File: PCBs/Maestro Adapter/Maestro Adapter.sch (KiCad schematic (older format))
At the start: 14 parts, among them J0 Conn_01x02_Female, J1 Conn_01x02_Female, J10 Conn_01x02_Female, J11 Conn_01x02_Female, J12 Conn_01x12_Male, J13 Conn_01x12_Male, J2 Conn_01x02_Female, J3 Conn_01x02_Female, J4 Conn_01x02_Female, J5 Conn_01x02_Female, J6 Conn_01x02_Female, J7 Conn_01x02_Female, J8 Conn_01x02_Female, J9 Conn_01x02_Female

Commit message: added spot for missed gap in servo channels
missed a gap between channel 5 and 6. so added additional pads
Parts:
- removed J12, J13: Conn_01x12_Male, through hole:1x12 through hole, symbol Connector:Conn_01x12_Male
- added J12, J13: Conn_01x13_Male, through hole:1x13 through hole, symbol Connector:Conn_01x13_Male
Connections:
- wire segments 45 -> 50
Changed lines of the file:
@@
 EESchema Schematic File Version 4
+LIBS:Maestro Adapter-cache
 EELAYER 26 0
 EELAYER END
@@
 $EndDescr
 $Comp
-L Connector:Conn_01x12_Male J13
-U 1 1 5BCE744C
-P 1550 3800
-F 0 "J13" H 1656 4478 50  0000 C CNN
-F 1 "Conn_01x12_Male" H 1656 4387 50  0000 C CNN
-F 2 "through hole:1x12 through hole" H 1550 3800 50  0001 C CNN
-F 3 "~" H 1550 3800 50  0001 C CNN
-	1    1550 3800
-	1    0    0    -1
-$EndComp
-$Comp
-L Connector:Conn_01x12_Male J12
-U 1 1 5BCE74E8
-P 2400 3800
-F 0 "J12" H 2506 4478 50  0000 C CNN
-F 1 "Conn_01x12_Male" H 2506 4387 50  0000 C CNN
-F 2 "through hole:1x12 through hole" H 2400 3800 50  0001 C CNN
-F 3 "~" H 2400 3800 50  0001 C CNN
-	1    2400 3800
-	1    0    0    -1
-$EndComp
-$Comp
 L Connector:Conn_01x02_Female J11
 U 1 1 5BCE7753
@@
 Text GLabel 4150 2700 0    50   Input ~ 0
 GND
-Wire Wire Line
-	1750 3300 1750 3400
-Connection ~ 1750 3400
-Wire Wire Line
-	1750 3400 1750 3500
-Connection ~ 1750 3500
-Wire Wire Line
-	1750 3500 1750 3600
-Connection ~ 1750 3600
-Wire Wire Line
-	1750 3600 1750 3700
-Connection ~ 1750 3700
-Wire Wire Line
-	1750 3700 1750 3800
-Connection ~ 1750 3800
-Wire Wire Line
-	1750 3800 1750 3900
-Connection ~ 1750 3900
-Wire Wire Line
-	1750 3900 1750 4000
-Connection ~ 1750 4000
-Wire Wire Line
-	1750 4000 1750 4100
-Connection ~ 1750 4100
-Wire Wire Line
-	1750 4100 1750 4200
-Connection ~ 1750 4200
-Wire Wire Line
-	1750 4200 1750 4300
-Connection ~ 1750 4300
-Wire Wire Line
-	1750 4300 1750 4400
 Text GLabel 1750 4400 3    50   Input ~ 0
 GND
@@
 Wire Wire Line
 	3250 3400 4150 3400
-Wire Wire Line
-	2600 3800 3350 3800
-Wire Wire Line
-	3350 3800 3350 3600
-Wire Wire Line
-	3350 3600 4150 3600
-Wire Wire Line
-	2600 3900 3450 3900
-Wire Wire Line
-	3450 3900 3450 3800
-Wire Wire Line
-	3450 3800 4150 3800
-Wire Wire Line
-	2600 4000 4150 4000
-Wire Wire Line
-	2600 4100 3450 4100
-Wire Wire Line
-	3450 4100 3450 4200
-Wire Wire Line
-	3450 4200 4150 4200
-Wire Wire Line
-	2600 4200 3350 4200
-Wire Wire Line
-	3350 4200 3350 4400
-Wire Wire Line
-	3350 4400 4150 4400
-Wire Wire Line
-	2600 4300 3250 4300
-Wire Wire Line
-	3250 4300 3250 4600
-Wire Wire Line
-	3250 4600 4150 4600
-Wire Wire Line
-	2600 4400 3150 4400
-Wire Wire Line
-	3150 4400 3150 4800
-Wire Wire Line
-	3150 4800 4150 4800
 $Bitmap
 Pos 9100 6900
@@
 EndData
 $EndBitmap
+$Comp
+L Connector:Conn_01x13_Male J12
+U 1 1 5BCF052F
+P 2400 3900
+F 0 "J12" H 2506 4678 50  0000 C CNN
+F 1 "Conn_01x13_Male" H 2506 4587 50  0000 C CNN
+F 2 "through hole:1x13 through hole" H 2400 3900 50  0001 C CNN
+F 3 "~" H 2400 3900 50  0001 C CNN
+	1    2400 3900
+	1    0    0    -1
+$EndComp
+$Comp
+L Connector:Conn_01x13_Male J13
+U 1 1 5BCF059F
+P 1550 3800
+F 0 "J13" H 1656 4578 50  0000 C CNN
+F 1 "Conn_01x13_Male" H 1656 4487 50  0000 C CNN
+F 2 "through hole:1x13 through hole" H 1550 3800 50  0001 C CNN
+F 3 "~" H 1550 3800 50  0001 C CNN
+	1    1550 3800
+	1    0    0    -1
+$EndComp
+Wire Wire Line
+	2600 4500 2800 4500
+Wire Wire Line
+	2800 4500 2800 4800
+Wire Wire Line
+	2800 4800 4150 4800
+Wire Wire Line
+	2600 4400 2900 4400
+Wire Wire Line
+	2900 4400 2900 4600
+Wire Wire Line
+	2900 4600 4150 4600
+Wire Wire Line
+	2600 4300 3000 4300
+Wire Wire Line
+	3000 4300 3000 4400
+Wire Wire Line
+	3000 4400 4150 4400
+Wire Wire Line
+	2600 4200 4150 4200
+Wire Wire Line
+	2600 4100 3000 4100
+Wire Wire Line
+	3000 4100 3000 4000
+Wire Wire Line
+	3000 4000 4150 4000
+Wire Wire Line
+	2600 4000 2950 4000
+Wire Wire Line
+	2950 4000 2950 3900
+Wire Wire Line
+	2950 3900 3850 3900
+Wire Wire Line
+	3850 3900 3850 3800
+Wire Wire Line
+	3850 3800 4150 3800
+Wire Wire Line
+	2600 3900 2850 3900
+Wire Wire Line
+	2850 3900 2850 3800
+Wire Wire Line
+	2850 3800 3750 3800
+Wire Wire Line
+	3750 3800 3750 3600
+Wire Wire Line
+	3750 3600 4150 3600
+Wire Wire Line
+	1750 3200 1750 3300
+Connection ~ 1750 3300
+Wire Wire Line
+	1750 3300 1750 3400
+Connection ~ 1750 3400
+Wire Wire Line
+	1750 3400 1750 3500
+Connection ~ 1750 3500
+Wire Wire Line
+	1750 3500 1750 3600
+Connection ~ 1750 3600
+Wire Wire Line
+	1750 3600 1750 3700
+Connection ~ 1750 3700
+Wire Wire Line
+	1750 3700 1750 3800
+Connection ~ 1750 3800
+Wire Wire Line
+	1750 3800 1750 3900
+Connection ~ 1750 3900
+Wire Wire Line
+	1750 3900 1750 4000
+Connection ~ 1750 4000
+Wire Wire Line
+	1750 4000 1750 4100
+Connection ~ 1750 4100
+Wire Wire Line
+	1750 4100 1750 4200
+Connection ~ 1750 4200
+Wire Wire Line
+	1750 4200 1750 4300
+Connection ~ 1750 4300
+Wire Wire Line
+	1750 4300 1750 4400
 $EndSCHEMATC

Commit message: Added Colour to 3D Model
We probably have to change the footprint again anyways, but at least now its in colour!!!
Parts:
- J0, J1, J10, J11, J2, J3, J4, J5, J6, J7, J8, J9: footprint through hole:1x2_molex_llc -> EER:1x2_molex_llc
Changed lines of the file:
@@
 F 0 "J11" H 4377 2576 50  0000 L CNN
 F 1 "Conn_01x02_Female" H 4377 2485 50  0000 L CNN
-F 2 "through hole:1x2_molex_llc" H 4350 2600 50  0001 C CNN
+F 2 "EER:1x2_molex_llc" H 4350 2600 50  0001 C CNN
 F 3 "~" H 4350 2600 50  0001 C CNN
 	1    4350 2600
@@
 F 0 "J10" H 4377 2776 50  0000 L CNN
 F 1 "Conn_01x02_Female" H 4377 2685 50  0000 L CNN
-F 2 "through hole:1x2_molex_llc" H 4350 2800 50  0001 C CNN
+F 2 "EER:1x2_molex_llc" H 4350 2800 50  0001 C CNN
 F 3 "~" H 4350 2800 50  0001 C CNN
 	1    4350 2800
@@
 F 0 "J9" H 4377 2976 50  0000 L CNN
 F 1 "Conn_01x02_Female" H 4377 2885 50  0000 L CNN
-F 2 "through hole:1x2_molex_llc" H 4350 3000 50  0001 C CNN
+F 2 "EER:1x2_molex_llc" H 4350 3000 50  0001 C CNN
 F 3 "~" H 4350 3000 50  0001 C CNN
 	1    4350 3000
@@
 F 0 "J8" H 4377 3176 50  0000 L CNN
 F 1 "Conn_01x02_Female" H 4377 3085 50  0000 L CNN
-F 2 "through hole:1x2_molex_llc" H 4350 3200 50  0001 C CNN
+F 2 "EER:1x2_molex_llc" H 4350 3200 50  0001 C CNN
 F 3 "~" H 4350 3200 50  0001 C CNN
 	1    4350 3200
@@
 F 0 "J7" H 4377 3376 50  0000 L CNN
 F 1 "Conn_01x02_Female" H 4377 3285 50  0000 L CNN
-F 2 "through hole:1x2_molex_llc" H 4350 3400 50  0001 C CNN
+F 2 "EER:1x2_molex_llc" H 4350 3400 50  0001 C CNN
 F 3 "~" H 4350 3400 50  0001 C CNN
 	1    4350 3400
@@
 F 0 "J6" H 4377 3576 50  0000 L CNN
 F 1 "Conn_01x02_Female" H 4377 3485 50  0000 L CNN
-F 2 "through hole:1x2_molex_llc" H 4350 3600 50  0001 C CNN
+F 2 "EER:1x2_molex_llc" H 4350 3600 50  0001 C CNN
 F 3 "~" H 4350 3600 50  0001 C CNN
 	1    4350 3600
@@
 F 0 "J5" H 4377 3776 50  0000 L CNN
 F 1 "Conn_01x02_Female" H 4377 3685 50  0000 L CNN
-F 2 "through hole:1x2_molex_llc" H 4350 3800 50  0001 C CNN
+F 2 "EER:1x2_molex_llc" H 4350 3800 50  0001 C CNN
 F 3 "~" H 4350 3800 50  0001 C CNN
 	1    4350 3800
@@
 F 0 "J4" H 4377 3976 50  0000 L CNN
 F 1 "Conn_01x02_Female" H 4377 3885 50  0000 L CNN
-F 2 "through hole:1x2_molex_llc" H 4350 4000 50  0001 C CNN
+F 2 "EER:1x2_molex_llc" H 4350 4000 50  0001 C CNN
 F 3 "~" H 4350 4000 50  0001 C CNN
 	1    4350 4000
@@
 F 0 "J3" H 4377 4176 50  0000 L CNN
 F 1 "Conn_01x02_Female" H 4377 4085 50  0000 L CNN
-F 2 "through hole:1x2_molex_llc" H 4350 4200 50  0001 C CNN
+F 2 "EER:1x2_molex_llc" H 4350 4200 50  0001 C CNN
 F 3 "~" H 4350 4200 50  0001 C CNN
 	1    4350 4200
@@
 F 0 "J2" H 4377 4376 50  0000 L CNN
 F 1 "Conn_01x02_Female" H 4377 4285 50  0000 L CNN
-F 2 "through hole:1x2_molex_llc" H 4350 4400 50  0001 C CNN
+F 2 "EER:1x2_molex_llc" H 4350 4400 50  0001 C CNN
 F 3 "~" H 4350 4400 50  0001 C CNN
 	1    4350 4400
@@
 F 0 "J1" H 4377 4576 50  0000 L CNN
 F 1 "Conn_01x02_Female" H 4377 4485 50  0000 L CNN
-F 2 "through hole:1x2_molex_llc" H 4350 4600 50  0001 C CNN
+F 2 "EER:1x2_molex_llc" H 4350 4600 50  0001 C CNN
 F 3 "~" H 4350 4600 50  0001 C CNN
 	1    4350 4600
@@
 F 0 "J0" H 4377 4776 50  0000 L CNN
 F 1 "Conn_01x02_Female" H 4377 4685 50  0000 L CNN
-F 2 "through hole:1x2_molex_llc" H 4350 4800 50  0001 C CNN
+F 2 "EER:1x2_molex_llc" H 4350 4800 50  0001 C CNN
 F 3 "~" H 4350 4800 50  0001 C CNN
 	1    4350 4800

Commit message: Completed List of suggestions
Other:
- moved on the sheet: J13
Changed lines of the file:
@@
 	1    0    0    -1
 $EndComp
-Text GLabel 4150 2700 0    50   Input ~ 0
-GND
-Text GLabel 1750 4400 3    50   Input ~ 0
-GND
 $Comp
 L Connector:Conn_01x02_Female J10
@@
 	1    0    0    -1
 $EndComp
-Text GLabel 4150 2900 0    50   Input ~ 0
-GND
 $Comp
 L Connector:Conn_01x02_Female J9
@@
 	1    0    0    -1
 $EndComp
-Text GLabel 4150 3100 0    50   Input ~ 0
-GND
 $Comp
 L Connector:Conn_01x02_Female J8
@@
 	1    0    0    -1
 $EndComp
-Text GLabel 4150 3300 0    50   Input ~ 0
-GND
 $Comp
 L Connector:Conn_01x02_Female J7
@@
 	1    0    0    -1
 $EndComp
-Text GLabel 4150 3500 0    50   Input ~ 0
-GND
 $Comp
 L Connector:Conn_01x02_Female J6
@@
 	1    0    0    -1
 $EndComp
-Text GLabel 4150 3700 0    50   Input ~ 0
-GND
 $Comp
 L Connector:Conn_01x02_Female J5
@@
 	1    0    0    -1
 $EndComp
-Text GLabel 4150 3900 0    50   Input ~ 0
-GND
 $Comp
 L Connector:Conn_01x02_Female J4
@@
 	1    0    0    -1
 $EndComp
-Text GLabel 4150 4100 0    50   Input ~ 0
-GND
 $Comp
 L Connector:Conn_01x02_Female J3
@@
 	1    0    0    -1
 $EndComp
-Text GLabel 4150 4300 0    50   Input ~ 0
-GND
 $Comp
 L Connector:Conn_01x02_Female J2
@@
 	1    0    0    -1
 $EndComp
-Text GLabel 4150 4500 0    50   Input ~ 0
-GND
 $Comp
 L Connector:Conn_01x02_Female J1
@@
 	1    0    0    -1
 $EndComp
-Text GLabel 4150 4700 0    50   Input ~ 0
-GND
 $Comp
 L Connector:Conn_01x02_Female J0
@@
 	1    0    0    -1
 $EndComp
-Text GLabel 4150 4900 0    50   Input ~ 0
-GND
 Wire Wire Line
 	2600 3300 2850 3300
@@
 L Connector:Conn_01x13_Male J13
 U 1 1 5BCF059F
-P 1550 3800
-F 0 "J13" H 1656 4578 50  0000 C CNN
-F 1 "Conn_01x13_Male" H 1656 4487 50  0000 C CNN
-F 2 "through hole:1x13 through hole" H 1550 3800 50  0001 C CNN
-F 3 "~" H 1550 3800 50  0001 C CNN
-	1    1550 3800
+P 1700 3900
+F 0 "J13" H 1806 4678 50  0000 C CNN
+F 1 "Conn_01x13_Male" H 1806 4587 50  0000 C CNN
+F 2 "through hole:1x13 through hole" H 1700 3900 50  0001 C CNN
+F 3 "~" H 1700 3900 50  0001 C CNN
+	1    1700 3900
 	1    0    0    -1
 $EndComp
@@
 	3750 3600 4150 3600
 Wire Wire Line
-	1750 3200 1750 3300
-Connection ~ 1750 3300
-Wire Wire Line
-	1750 3300 1750 3400
-Connection ~ 1750 3400
-Wire Wire Line
-	1750 3400 1750 3500
-Connection ~ 1750 3500
-Wire Wire Line
-	1750 3500 1750 3600
-Connection ~ 1750 3600
-Wire Wire Line
-	1750 3600 1750 3700
-Connection ~ 1750 3700
-Wire Wire Line
-	1750 3700 1750 3800
-Connection ~ 1750 3800
-Wire Wire Line
-	1750 3800 1750 3900
-Connection ~ 1750 3900
-Wire Wire Line
-	1750 3900 1750 4000
-Connection ~ 1750 4000
-Wire Wire Line
-	1750 4000 1750 4100
-Connection ~ 1750 4100
-Wire Wire Line
-	1750 4100 1750 4200
-Connection ~ 1750 4200
-Wire Wire Line
-	1750 4200 1750 4300
-Connection ~ 1750 4300
-Wire Wire Line
-	1750 4300 1750 4400
+	1900 3300 1900 3400
+Connection ~ 1900 3400
+Wire Wire Line
+	1900 3400 1900 3500
+Connection ~ 1900 3500
+Wire Wire Line
+	1900 3500 1900 3600
+Connection ~ 1900 3600
+Wire Wire Line
+	1900 3600 1900 3700
+Connection ~ 1900 3700
+Wire Wire Line
+	1900 3700 1900 3800
+Connection ~ 1900 3800
+Wire Wire Line
+	1900 3800 1900 3900
+Connection ~ 1900 3900
+Wire Wire Line
+	1900 3900 1900 4000
+Connection ~ 1900 4000
+Wire Wire Line
+	1900 4000 1900 4100
+Connection ~ 1900 4100
+Wire Wire Line
+	1900 4100 1900 4200
+Connection ~ 1900 4200
+Wire Wire Line
+	1900 4200 1900 4300
+Connection ~ 1900 4300
+Wire Wire Line
+	1900 4300 1900 4400
+Connection ~ 1900 4400
+Wire Wire Line
+	1900 4400 1900 4500
+$Comp
+L power:GND #PWR0101
+U 1 1 5BCFD261
+P 1900 4500
+F 0 "#PWR0101" H 1900 4250 50  0001 C CNN
+F 1 "GND" H 1905 4327 50  0000 C CNN
+F 2 "" H 1900 4500 50  0001 C CNN
+F 3 "" H 1900 4500 50  0001 C CNN
+	1    1900 4500
+	1    0    0    -1
+$EndComp
+Connection ~ 1900 4500
+$Comp
+L power:GND #PWR0102
+U 1 1 5BCFD44A
+P 4150 2700
+F 0 "#PWR0102" H 4150 2450 50  0001 C CNN
+F 1 "GND" V 4155 2572 50  0000 R CNN
+F 2 "" H 4150 2700 50  0001 C CNN
+F 3 "" H 4150 2700 50  0001 C CNN
+	1    4150 2700
+	0    1    1    0
+$EndComp
+$Comp
+L power:GND #PWR0103
+U 1 1 5BCFD47F
+P 4150 2900
+F 0 "#PWR0103" H 4150 2650 50  0001 C CNN
+F 1 "GND" V 4155 2772 50  0000 R CNN
+F 2 "" H 4150 2900 50  0001 C CNN
+F 3 "" H 4150 2900 50  0001 C CNN
+	1    4150 2900
+	0    1    1    0
+$EndComp
+$Comp
+L power:GND #PWR0104
+U 1 1 5BCFD4B4
+P 4150 3100
+F 0 "#PWR0104" H 4150 2850 50  0001 C CNN
+F 1 "GND" V 4155 2972 50  0000 R CNN
+F 2 "" H 4150 3100 50  0001 C CNN
+F 3 "" H 4150 3100 50  0001 C CNN
+	1    4150 3100
+	0    1    1    0
+$EndComp
+$Comp
+L power:GND #PWR0105
+U 1 1 5BCFD4E9
+P 4150 3300
+F 0 "#PWR0105" H 4150 3050 50  0001 C CNN
+F 1 "GND" V 4155 3172 50  0000 R CNN
+F 2 "" H 4150 3300 50  0001 C CNN
+F 3 "" H 4150 3300 50  0001 C CNN
+	1    4150 3300
+	0    1    1    0
+$EndComp
+$Comp
+L power:GND #PWR0106
+U 1 1 5BCFD51E
+P 4150 3500
+F 0 "#PWR0106" H 4150 3250 50  0001 C CNN
+F 1 "GND" V 4155 3372 50  0000 R CNN
+F 2 "" H 4150 3500 50  0001 C CNN
+F 3 "" H 4150 3500 50  0001 C CNN
+	1    4150 3500
+	0    1    1    0
+$EndComp
+$Comp
+L power:GND #PWR0107
+U 1 1 5BCFD553
+P 4150 3700
+F 0 "#PWR0107" H 4150 3450 50  0001 C CNN
+F 1 "GND" V 4155 3572 50  0000 R CNN
+F 2 "" H 4150 3700 50  0001 C CNN
+F 3 "" H 4150 3700 50  0001 C CNN
+	1    4150 3700
+	0    1    1    0
+$EndComp
+$Comp
+L power:GND #PWR0108
+U 1 1 5BCFD588
+P 4150 3900
+F 0 "#PWR0108" H 4150 3650 50  0001 C CNN
+F 1 "GND" V 4155 3772 50  0000 R CNN
+F 2 "" H 4150 3900 50  0001 C CNN
+F 3 "" H 4150 3900 50  0001 C CNN
+	1    4150 3900
+	0    1    1    0
+$EndComp
+$Comp
+L power:GND #PWR0109
+U 1 1 5BCFD5BD
+P 4150 4100
+F 0 "#PWR0109" H 4150 3850 50  0001 C CNN
+F 1 "GND" V 4155 3972 50  0000 R CNN
+F 2 "" H 4150 4100 50  0001 C CNN
+F 3 "" H 4150 4100 50  0001 C CNN
+	1    4150 4100
+	0    1    1    0
+$EndComp
+$Comp
+L power:GND #PWR0110
+U 1 1 5BCFD5F2
+P 4150 4300
+F 0 "#PWR0110" H 4150 4050 50  0001 C CNN
+F 1 "GND" V 4155 4172 50  0000 R CNN
+F 2 "" H 4150 4300 50  0001 C CNN
+F 3 "" H 4150 4300 50  0001 C CNN
+	1    4150 4300
+	0    1    1    0
+$EndComp
+$Comp
+L power:GND #PWR0111
+U 1 1 5BCFD627
+P 4150 4500
+F 0 "#PWR0111" H 4150 4250 50  0001 C CNN
+F 1 "GND" V 4155 4372 50  0000 R CNN
+F 2 "" H 4150 4500 50  0001 C CNN
+F 3 "" H 4150 4500 50  0001 C CNN
+	1    4150 4500
+	0    1    1    0
+$EndComp
+$Comp
+L power:GND #PWR0112
+U 1 1 5BCFD65C
+P 4150 4700
+F 0 "#PWR0112" H 4150 4450 50  0001 C CNN
+F 1 "GND" V 4155 4572 50  0000 R CNN
+F 2 "" H 4150 4700 50  0001 C CNN
+F 3 "" H 4150 4700 50  0001 C CNN
+	1    4150 4700
+	0    1    1    0
+$EndComp
+$Comp
+L power:GND #PWR0113
+U 1 1 5BCFD691
+P 4150 4900
+F 0 "#PWR0113" H 4150 4650 50  0001 C CNN
+F 1 "GND" V 4155 4772 50  0000 R CNN
+F 2 "" H 4150 4900 50  0001 C CNN
+F 3 "" H 4150 4900 50  0001 C CNN
+	1    4150 4900
+	0    1    1    0
+$EndComp
 $EndSCHEMATC

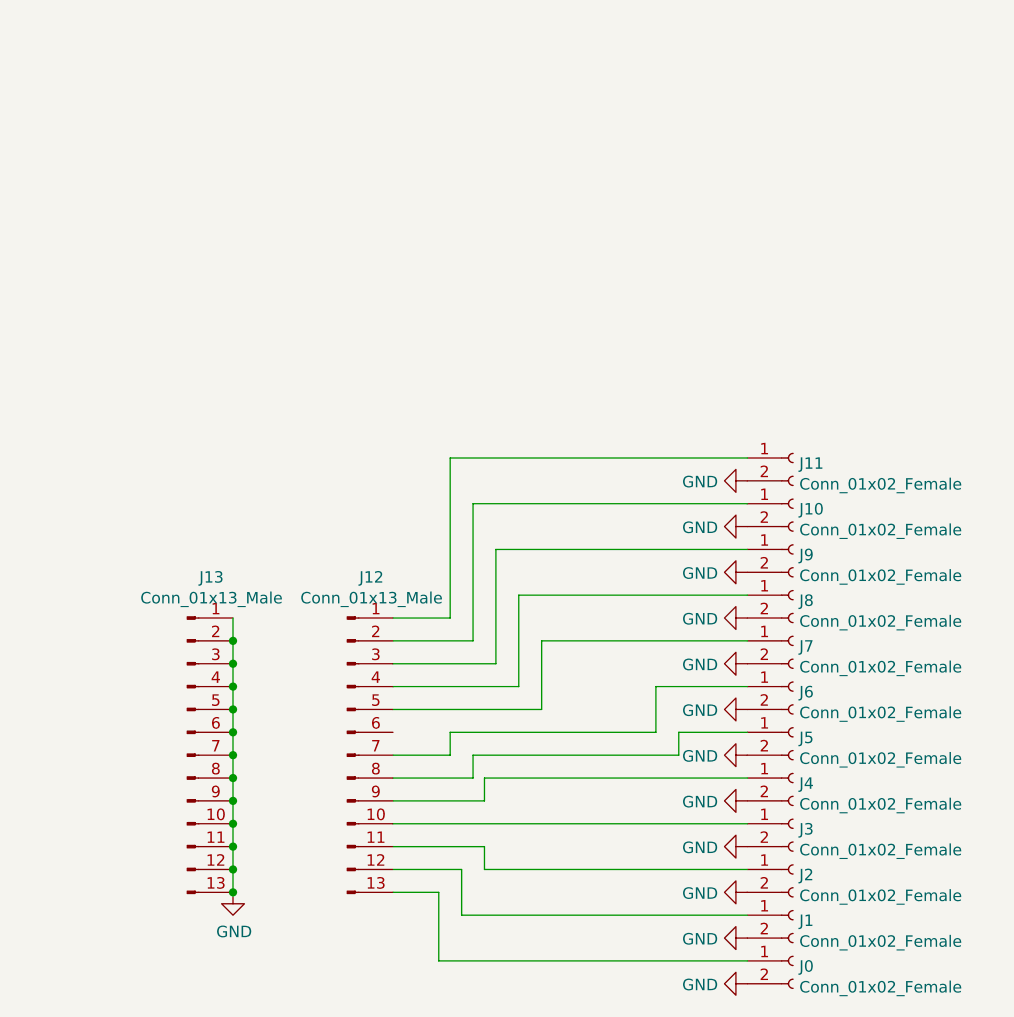
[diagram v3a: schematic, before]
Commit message: Converting to 18 channel maestro
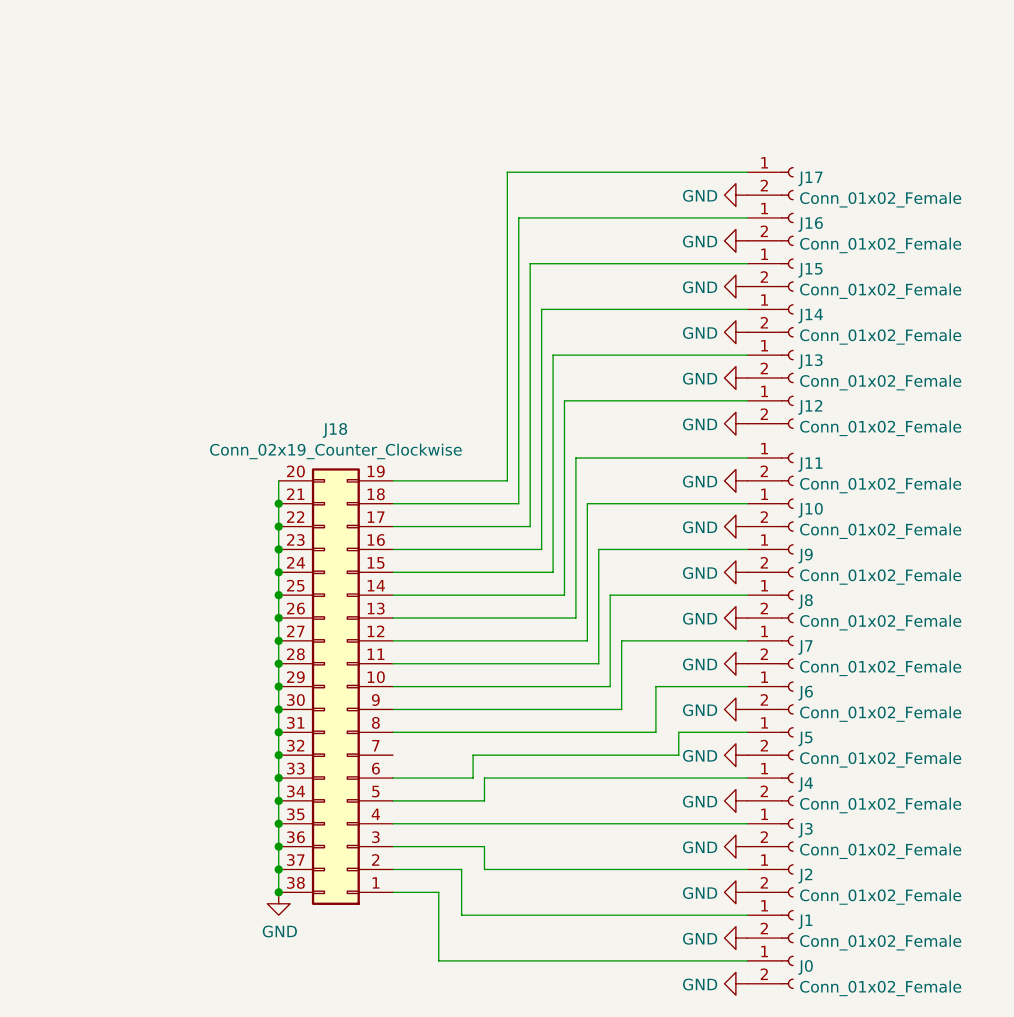
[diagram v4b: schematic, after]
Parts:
- removed J12, J13: Conn_01x13_Male, through hole:1x13 through hole, symbol Connector:Conn_01x13_Male
- added J12, J13, J14, J15, J16, J17: Conn_01x02_Female, EER:1x2_molex_llc, symbol Connector:Conn_01x02_Female
- added J18: Conn_02x19_Counter_Clockwise, EER:18ChannelMaestro, symbol Connector_Generic:Conn_02x19_Counter_Clockwise
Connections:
- net GND: now also J12.2 (Pin_2), J13.2 (Pin_2), J14.2 (Pin_2), J15.2 (Pin_2), J16.2 (Pin_2), J17.2 (Pin_2), J18.20 (Pin_20), J18.21 (Pin_21), J18.22 (Pin_22), J18.23 (Pin_23), J18.24 (Pin_24), J18.25 (Pin_25), J18.26 (Pin_26), J18.27 (Pin_27), J18.28 (Pin_28), J18.29 (Pin_29), J18.30 (Pin_30), J18.31 (Pin_31), J18.32 (Pin_32), J18.33 (Pin_33), J18.34 (Pin_34), J18.35 (Pin_35), J18.36 (Pin_36), J18.37 (Pin_37), J18.38 (Pin_38)
- net at J11.1 (Pin_1): now also J18.13 (Pin_13)
- net at J10.1 (Pin_1): now also J18.12 (Pin_12)
- net at J9.1 (Pin_1): now also J18.11 (Pin_11)
- net at J8.1 (Pin_1): now also J18.10 (Pin_10)
- net at J7.1 (Pin_1): now also J18.9 (Pin_9)
- net at J6.1 (Pin_1): now also J18.8 (Pin_8)
- net at J5.1 (Pin_1): now also J18.6 (Pin_6)
- net at J4.1 (Pin_1): now also J18.5 (Pin_5)
- net at J3.1 (Pin_1): now also J18.4 (Pin_4)
- net at J2.1 (Pin_1): now also J18.3 (Pin_3)
- net at J1.1 (Pin_1): now also J18.2 (Pin_2)
- net at J0.1 (Pin_1): now also J18.1 (Pin_1)
- new net: J12.1 (Pin_1), J18.14 (Pin_14)
- new net: J13.1 (Pin_1), J18.15 (Pin_15)
- new net: J14.1 (Pin_1), J18.16 (Pin_16)
- new net: J15.1 (Pin_1), J18.17 (Pin_17)
- new net: J16.1 (Pin_1), J18.18 (Pin_18)
- new net: J17.1 (Pin_1), J18.19 (Pin_19)

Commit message: Added led and resistor pads
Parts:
- added D1: LED, LED_SMD:LED_0805_2012Metric, symbol Device:LED
- added R1: R, Resistor_SMD:R_0201_0603Metric, symbol Device:R
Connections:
- net GND: now also D1.1 (K)
- net +5V: now reaches J18.7 (Pin_7)
- net +5V: now also R1.1
- new net: D1.2 (A), R1.2
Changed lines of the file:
@@
 $EndComp
 Connection ~ 2100 4500
+$Comp
+L power:+5V #PWR0120
+U 1 1 5BD48154
+P 2600 3900
+F 0 "#PWR0120" H 2600 3750 50  0001 C CNN
+F 1 "+5V" V 2615 4028 50  0000 L CNN
+F 2 "" H 2600 3900 50  0001 C CNN
+F 3 "" H 2600 3900 50  0001 C CNN
+	1    2600 3900
+	0    1    1    0
+$EndComp
+$Comp
+L Device:R R1
+U 1 1 5BD483A8
+P 1250 1150
+F 0 "R1" H 1320 1196 50  0000 L CNN
+F 1 "R" H 1320 1105 50  0000 L CNN
+F 2 "Resistor_SMD:R_0201_0603Metric" V 1180 1150 50  0001 C CNN
+F 3 "~" H 1250 1150 50  0001 C CNN
+	1    1250 1150
+	1    0    0    -1
+$EndComp
+$Comp
+L Device:LED D1
+U 1 1 5BD48430
+P 1250 1450
+F 0 "D1" V 1288 1333 50  0000 R CNN
+F 1 "LED" V 1197 1333 50  0000 R CNN
+F 2 "LED_SMD:LED_0805_2012Metric" H 1250 1450 50  0001 C CNN
+F 3 "~" H 1250 1450 50  0001 C CNN
+	1    1250 1450
+	0    -1   -1   0
+$EndComp
+$Comp
+L power:+5V #PWR0121
+U 1 1 5BD484FA
+P 1250 1000
+F 0 "#PWR0121" H 1250 850 50  0001 C CNN
+F 1 "+5V" H 1265 1173 50  0000 C CNN
+F 2 "" H 1250 1000 50  0001 C CNN
+F 3 "" H 1250 1000 50  0001 C CNN
+	1    1250 1000
+	1    0    0    -1
+$EndComp
+$Comp
+L power:GND #PWR0122
+U 1 1 5BD48554
+P 1250 1600
+F 0 "#PWR0122" H 1250 1350 50  0001 C CNN
+F 1 "GND" H 1255 1427 50  0000 C CNN
+F 2 "" H 1250 1600 50  0001 C CNN
+F 3 "" H 1250 1600 50  0001 C CNN
+	1    1250 1600
+	1    0    0    -1
+$EndComp
 $EndSCHEMATC
